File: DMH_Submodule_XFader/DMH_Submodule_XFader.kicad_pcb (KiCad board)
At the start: 2 copper layers, 37.5 x 62.5 mm, 47 parts, among them J1 Conn_01x08, J2 Conn_01x04, Q1 BC548, Q2 BC548, Q3 BC548, Q4 BC548, U1 TL074, U2 TL072

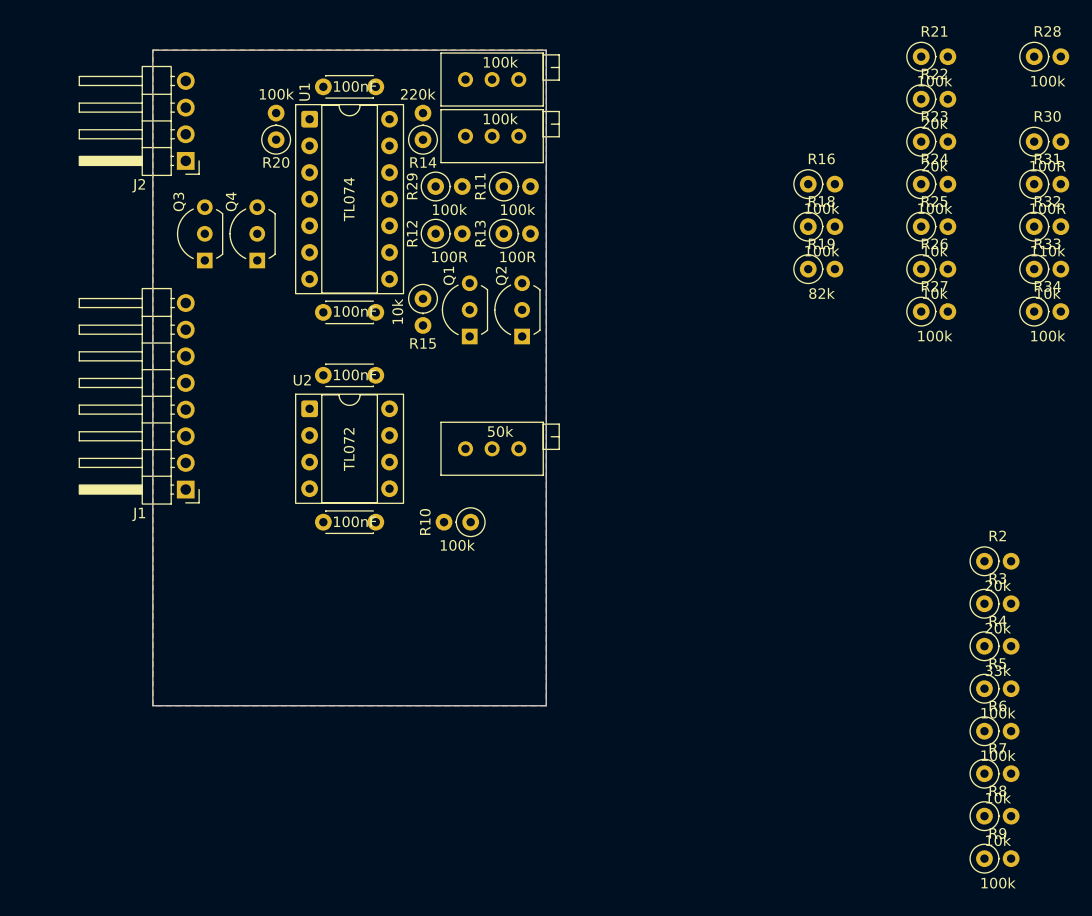
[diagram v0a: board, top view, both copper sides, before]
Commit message: Xfader comp placement done
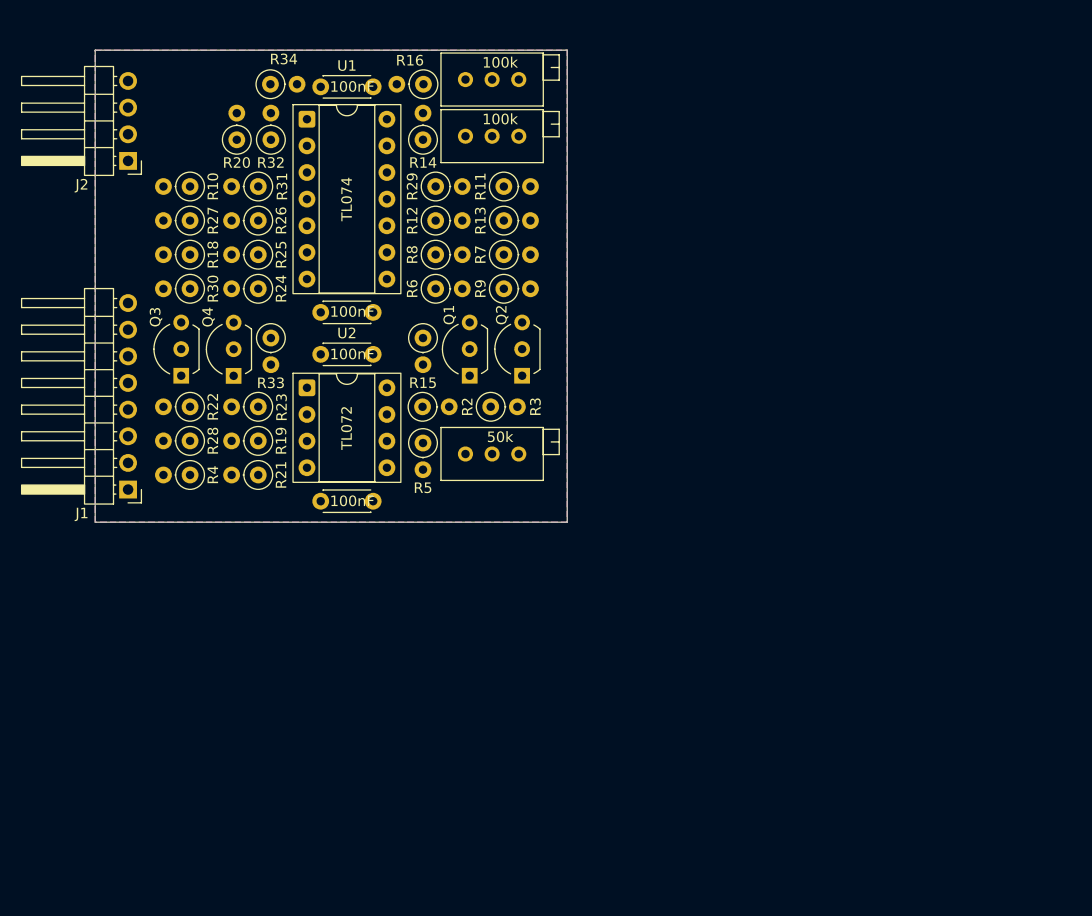
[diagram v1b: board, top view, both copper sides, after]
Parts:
- moved R28 88.4 mm to (63.5, 89.8), turned to 180 degrees
- moved R30 81.7 mm to (63.5, 75.2), turned to 180 degrees
- moved R4 77.5 mm to (63.5, 93.0), turned to 180 degrees
- moved R34 76.0 mm to (71.2, 55.8)
- moved R22 75.6 mm to (63.5, 86.5), turned to 180 degrees
- moved R8 74.8 mm to (87.0, 72.0)
- moved R21 74.7 mm to (70.0, 93.0), turned to 180 degrees
- moved R31 74.0 mm to (70.0, 65.5), turned to 180 degrees
- moved R32 73.2 mm to (71.2, 61.0), turned to 90 degrees
- moved R33 73.1 mm to (71.2, 79.9), turned to -90 degrees
- moved R9 71.1 mm to (93.5, 75.2)
- moved R27 70.2 mm to (63.5, 68.8), turned to 180 degrees
- moved R23 68.1 mm to (70.0, 86.5), turned to 180 degrees
- moved R7 67.4 mm to (93.5, 72.0)
- moved R6 67.2 mm to (87.0, 75.2)
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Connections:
- R18 pad 1: /Out A -> Net-(U2A--)
- R18 pad 2: Net-(U2A--) -> /Out A
- R2 pad 1: Net-(Q1-C) -> +12V
- R2 pad 2: +12V -> Net-(Q1-C)
- R21 pad 1: /Out A -> Net-(U2A--)
- R21 pad 2: Net-(U2A--) -> /Out A
- R22 pad 1: Net-(Q3-C) -> +12V
- R22 pad 2: +12V -> Net-(Q3-C)
- R23 pad 1: Net-(Q4-C) -> +12V
- R23 pad 2: +12V -> Net-(Q4-C)
- R3 pad 1: Net-(Q2-C) -> +12V
- R3 pad 2: +12V -> Net-(Q2-C)
- R4 pad 1: /CV Att In -> Net-(U2B--)
- R4 pad 2: Net-(U2B--) -> /CV Att In
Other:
- board size 37.5 x 62.5 mm -> 45 x 45 mm

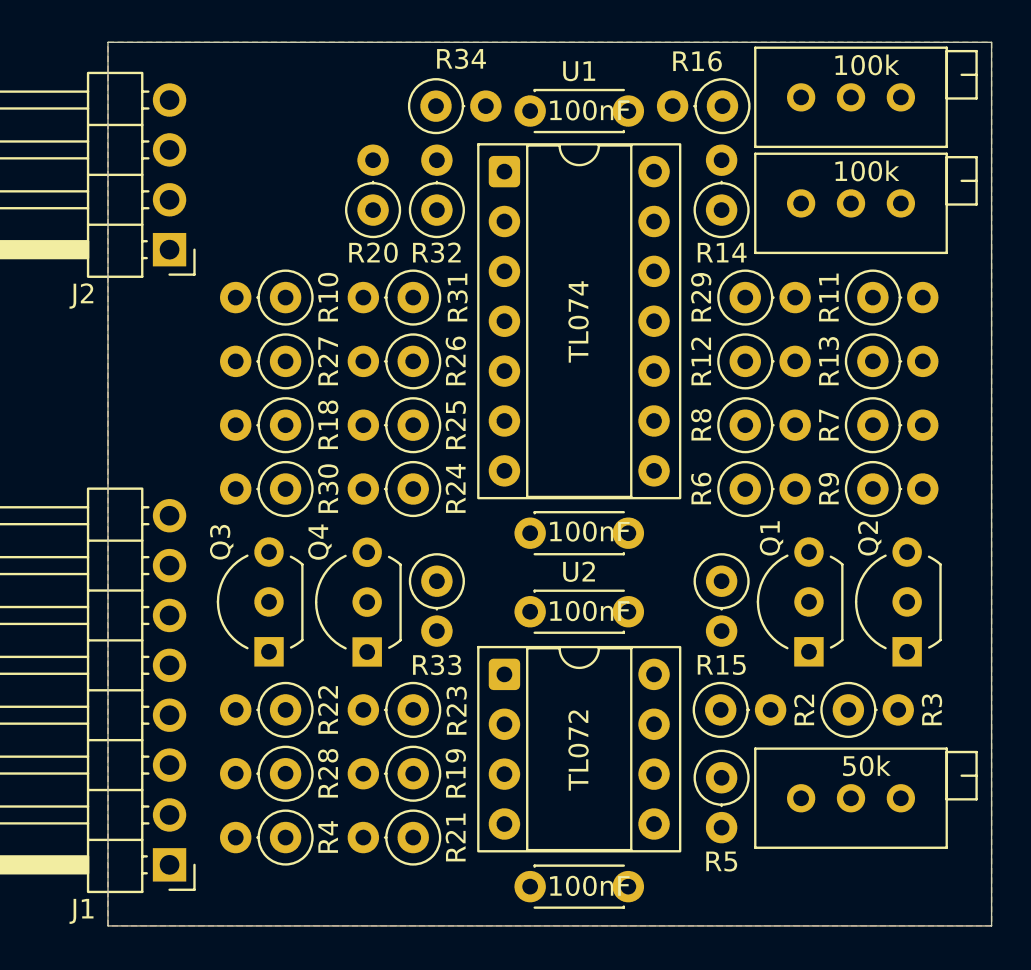
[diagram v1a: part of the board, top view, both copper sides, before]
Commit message: Xfader routing done
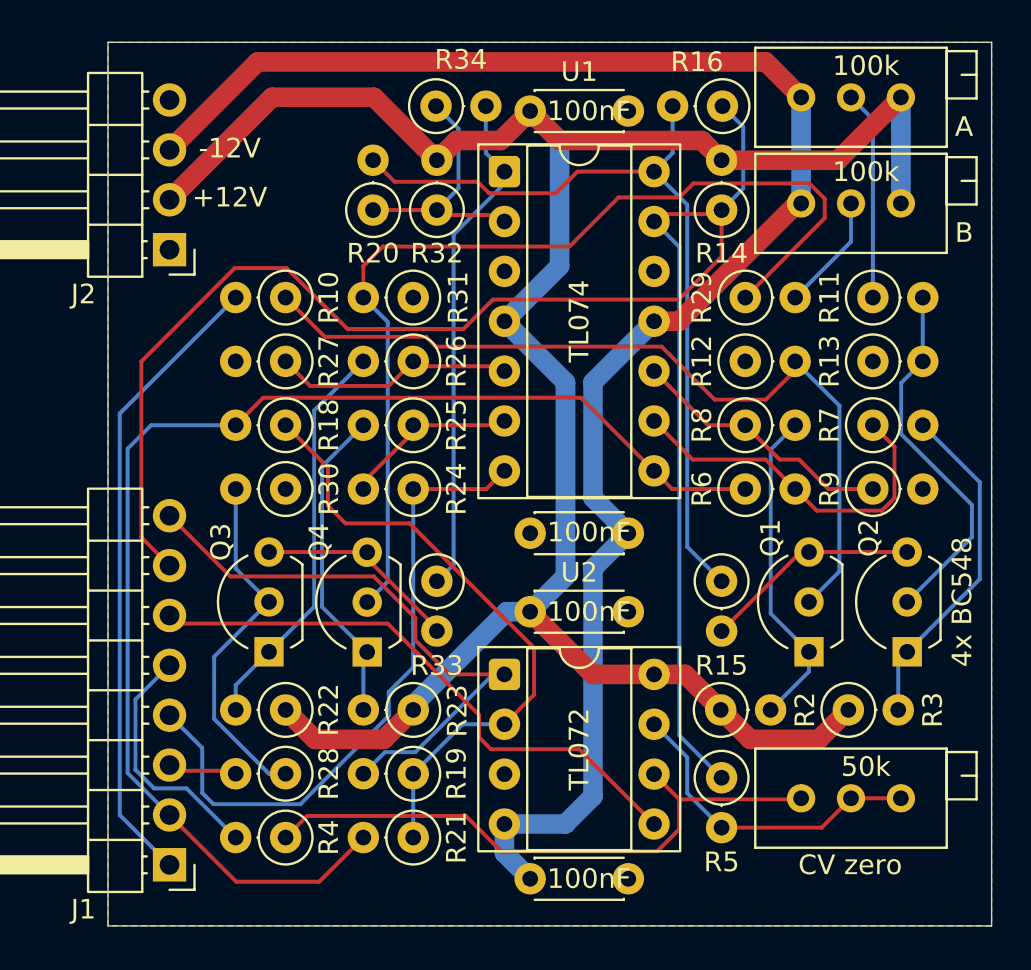
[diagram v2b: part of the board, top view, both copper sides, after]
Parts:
- moved C4 0.40 mm to (81.0, 95.1)
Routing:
- net +12V: track 0.00 -> 114.3 mm
- net /CV Mix In: track 0.00 -> 87.3 mm
- net -12V: track 0.00 -> 85.5 mm
- net /Out A: track 0.00 -> 66.2 mm
- net Net-(Q4-B): track 0.00 -> 50.3 mm
- net Net-(Q1-B): track 0.00 -> 43.0 mm
- net Net-(R15-Pad1): track 0.00 -> 41.5 mm
- net /Out B: track 0.00 -> 33.3 mm
- net /In A: track 0.00 -> 32.4 mm
- net Net-(U2A--): track 0.00 -> 31.9 mm
- net Net-(U2B--): track 0.00 -> 31.3 mm
- net /Out X: track 0.00 -> 30.3 mm
- net /CV Att Pot: track 0.00 -> 29.7 mm
- net Net-(R33-Pad1): track 0.00 -> 26.0 mm
- net Net-(Q3-C): track 0.00 -> 20.4 mm
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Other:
- board text added: "+12V"
- board text added: "-12V"
- board text added: "Mk1.0 - July 2026"
- board text removed: "Mk1.0 June 2026"

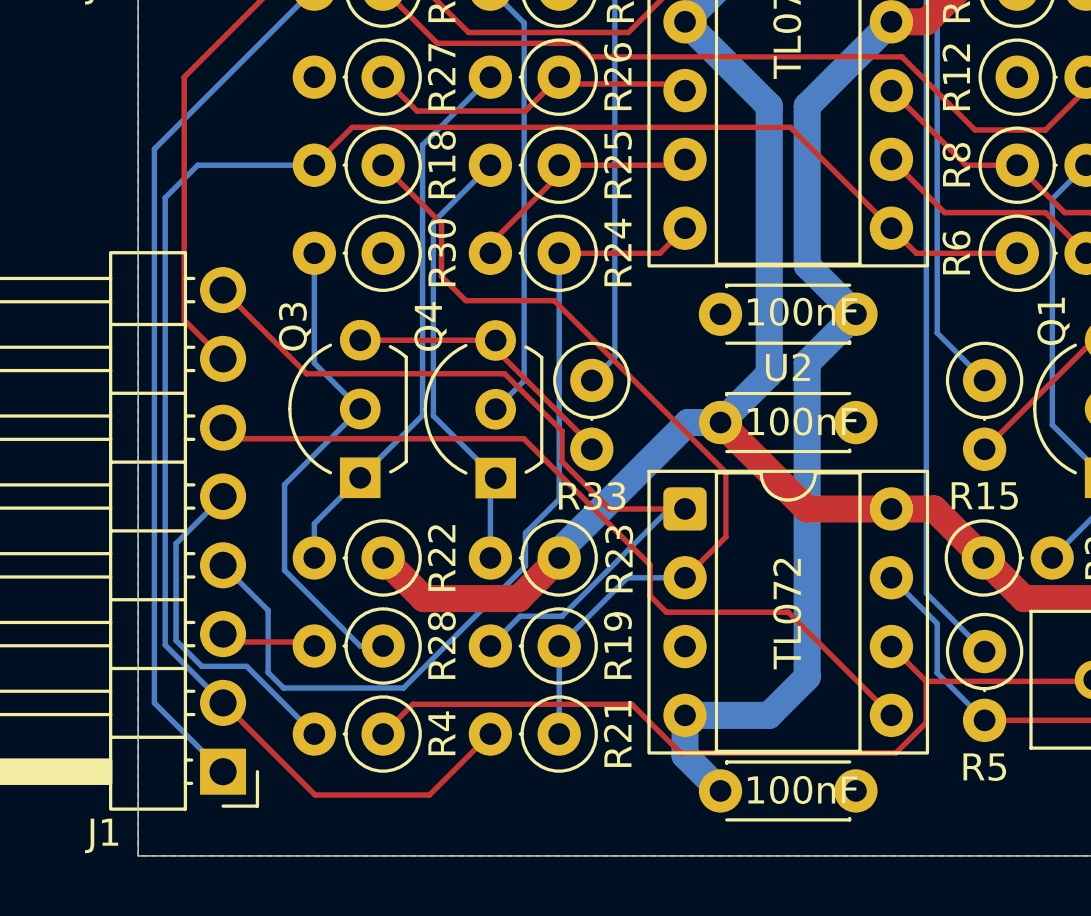
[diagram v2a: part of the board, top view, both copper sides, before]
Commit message: Fixed Out A and B mix labels and routing
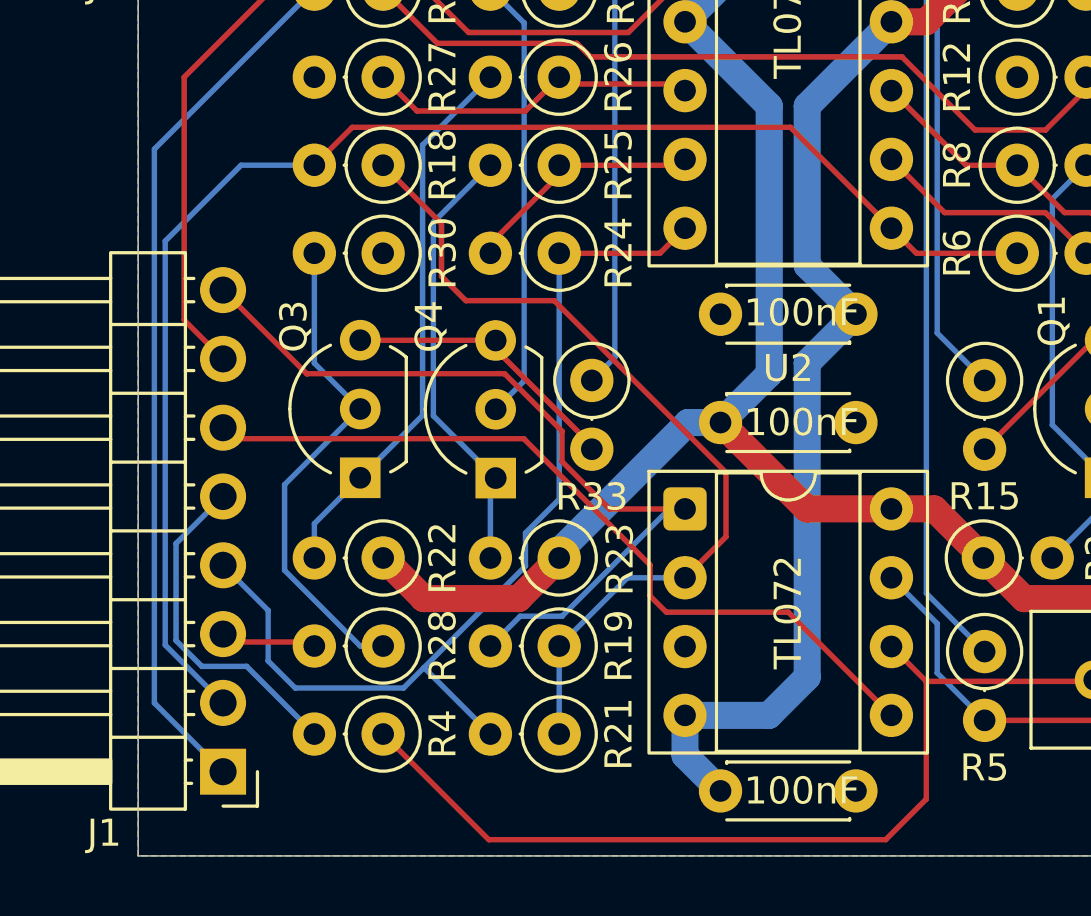
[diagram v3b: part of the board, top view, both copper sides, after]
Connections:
- net /CV Att In renamed /CV_Att_In
- net /CV Att Pot renamed /CV_Att_Pot
- net /CV Mix In renamed /CV_Mix_In
- net /In A renamed /In_A
- net /In B renamed /In_B
- net /Out X renamed /Out_X
- J1 pad 2: /Out A -> /Out_A
- J1 pad 4: /Out B -> /Out_B
- R18 pad 2: /Out A -> /Out_A
- R21 pad 2: /Out A -> /Out_B
- R24 pad 1: /Out B -> /Out_B
- R6 pad 1: /Out A -> /Out_A
- U1 pad 7: /Out B -> /Out_B
- U1 pad 8: /Out A -> /Out_A
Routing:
- net /Out A: track 66.2 -> 0.00 mm
- net /Out_A: track 0.00 -> 53.1 mm
- net /Out_B: track 0.00 -> 36.6 mm
- net /Out B: track 33.3 -> 0.00 mm
- net Net-(U2B--): track 31.3 -> 34.7 mm

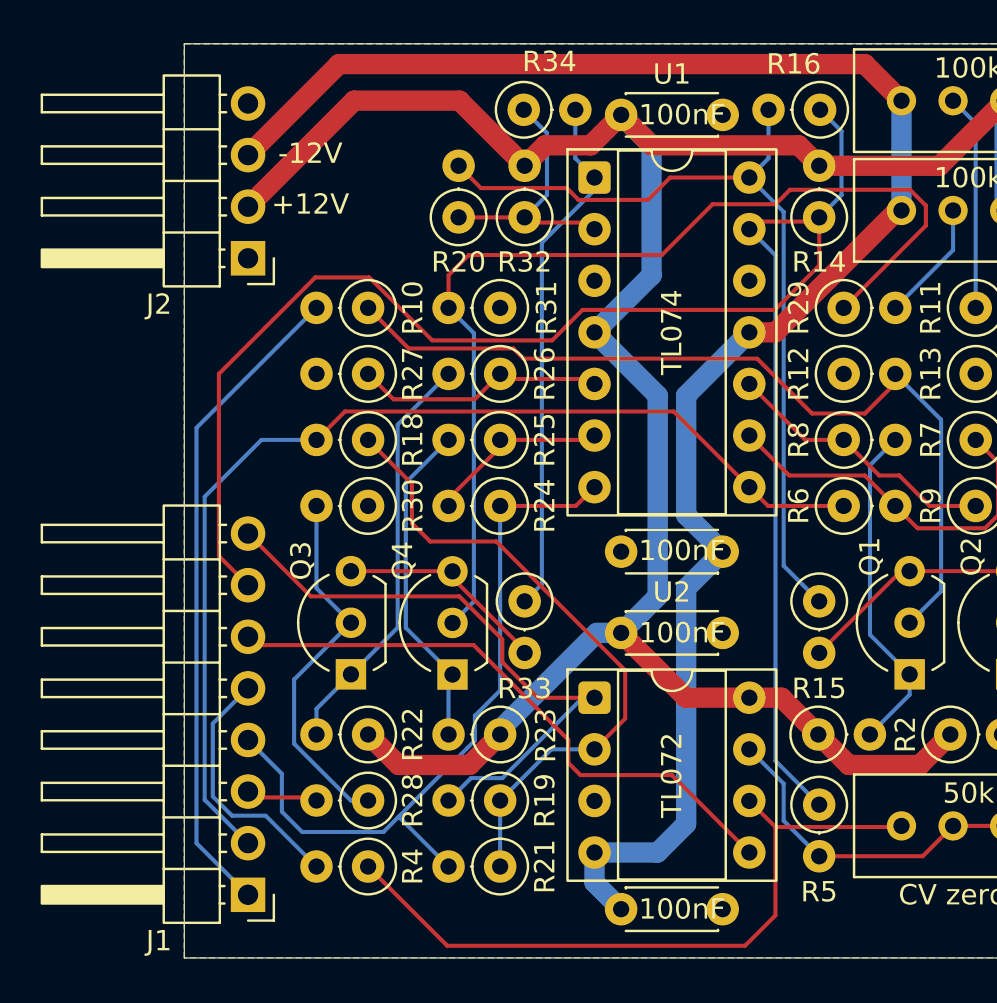
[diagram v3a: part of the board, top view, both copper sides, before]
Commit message: Made connector breadboard compatible
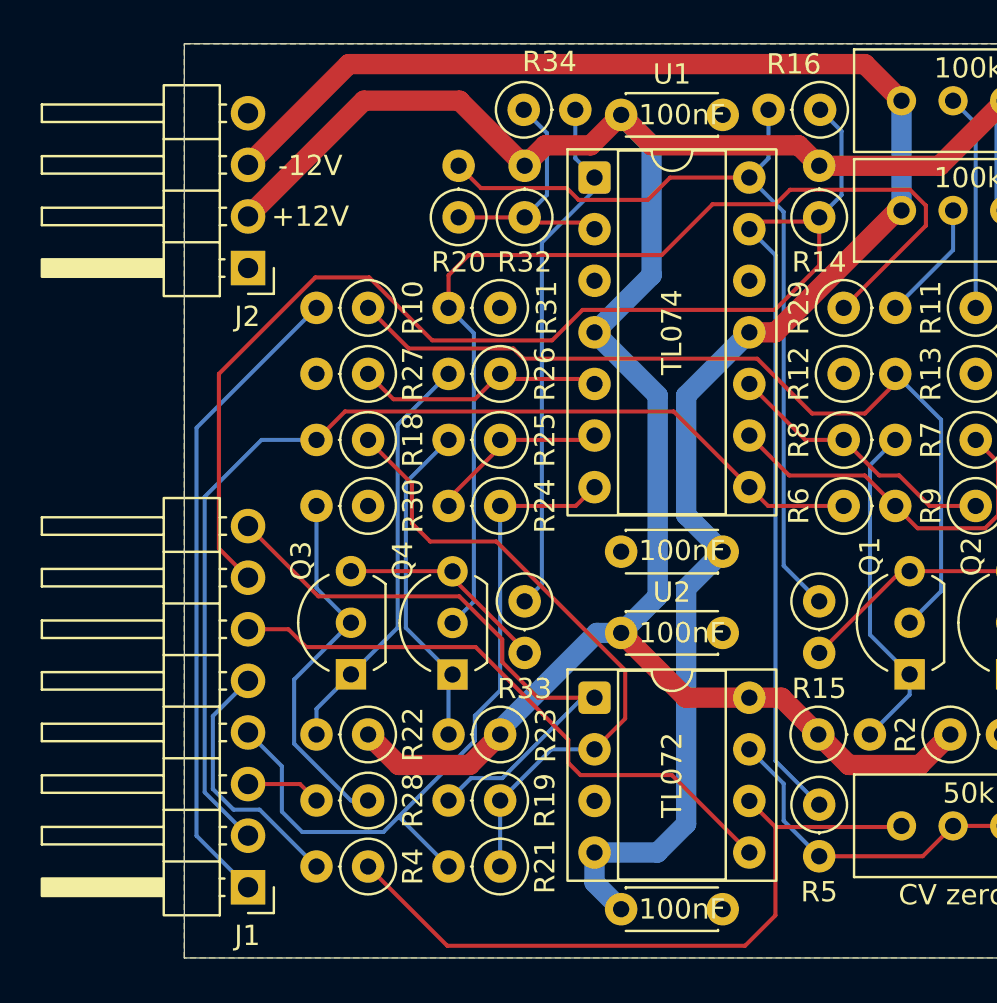
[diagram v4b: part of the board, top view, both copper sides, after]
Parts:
- moved J2 0.48 mm to (57.6, 63.5)
- moved J1 0.37 mm to (57.6, 94.0)

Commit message: Swapped J1 and J2 tags around on XFader SM
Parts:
- renumbered J2 to J1, J1 to J2
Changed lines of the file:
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@@
 	(paper "A4" portrait)
 	(title_block
+		(title "Cross Fader Submodule")
+		(date "2026-07-15")
 		(rev "1")
 		(company "DMH Instruments")
-		(comment 1 "10cm Kosmo format synthesizer module PCB")
+		(comment 1 "Submodule PCB for Kosmo format synthesizer module")
 	)
 	(layers
@@
 		(descr "Through hole angled pin header, 1x08, 2.54mm pitch, 6mm pin length, single row")
 		(tags "Through hole angled pin header THT 1x08 2.54mm single row")
-		(property "Reference" "J1"
+		(property "Reference" "J2"
 			(at 0.035 -2.38 0)
 			(layer "F.SilkS")
@@
 		(descr "Through hole angled pin header, 1x04, 2.54mm pitch, 6mm pin length, single row")
 		(tags "Through hole angled pin header THT 1x04 2.54mm single row")
-		(property "Reference" "J2"
+		(property "Reference" "J1"
 			(at 0.035 -2.39 0)
 			(layer "F.SilkS")
@@
 		)
 	)
+	(group "VC_Cross_Fader_SC"
+		(lib_id "SynthStuff:VC_Cross_Fader_SC")
+		(members "156aba6d-8716-4206-91db-de05616f5240" "15aec086-26ae-4e8f-a86d-fc440ad5c0df"
+			"1bb2db6c-582a-4b0e-8f4b-40b66a64ff61" "1fbbc819-05f1-47c2-8f1f-3bb8db341822"
+			"2b17a480-4af7-4e7f-991c-c097a11cd05d" "2e6d8948-6522-4f16-a307-ca4d9cc91755"
+			"30a23566-8bf4-4b6c-9b6a-75067ad19441" "369e710e-8de4-4dfb-ba15-73f4a77e019f"
+			"3956684d-cae4-4243-94fb-70f2736e98bc" "3d31149a-1864-4833-a03c-665f6cdabaeb"
+			"4461cd04-9275-4659-b197-4b0a686f2318" "56fed60b-4643-4708-9870-a6b837a88053"
+			"579d0aa6-73d9-4fb3-8abd-fc4274f45e4c" "583ccfeb-c872-4696-8f8f-0a6ca50f942c"
+			"5cca8f87-57cb-4272-b579-1a8804907ffc" "62c581da-ec56-4d57-96db-f129a8c06fc2"
+			"6a76fc0e-b09a-4e82-a521-1a4951e7ec7f" "6addff73-f2e9-4120-810d-7575553e364f"
+			"6c44f2a9-b4d8-40ea-8808-e1d65c021900" "7ae55dee-329c-4567-90b2-6424e93c5628"
+			"7bda555e-0de3-4edf-9854-241fcc90ec5e" "7c7e3e80-d168-4189-b051-6f808cd3f5fb"
+			"8320bda0-bc39-43a6-bfd5-06237ac0b623" "83eb8756-2e68-4a08-b851-e0782be10ee8"
+			"943f40ae-fc1c-4c4e-94ca-81dc930d78a3" "a59fb55c-dbe2-459e-b66d-08ceac7bc7c9"
+			"a6847c59-0b88-4466-8f82-91429cfb9da5" "a7a44be9-6090-4319-bec9-8a12132698da"
+			"ab5b8e30-2d71-4c6c-80ac-5a0302db4a4d" "ae2c829e-c655-4923-9b2f-7120f49f37bf"
+			"afca08c2-80c1-43d7-a743-0dc600a95ba6" "b1e27e14-d0ae-422f-8d6e-d1a523b2b754"
+			"b31ed478-7adb-466e-8d2f-699db136c7fa" "b9ee7b7e-a13e-4061-a12f-e3fcc1a05ca6"
+			"bce84751-ac23-4f29-8e5b-f7fc7d983cce" "c82e422e-f4c9-487b-a626-ad07bfc0854c"
+			"ca2998d3-202b-48cb-b112-83c1974e139a" "d63632fb-12e3-44c3-870f-47094aa139c1"
+			"d764697f-4978-448c-ae33-f1167d715a5b" "d9cee89f-b31c-41ec-8999-375c455e500d"
+			"ddebb524-a01e-48f0-9f1e-0a30325e7d16" "e8fcf28e-4c9d-4f11-a848-cb953976e413"
+			"e94f4345-b8fb-4abc-9fc7-42fb7c7bc8f3" "fc67f0af-7d82-489c-b288-521ec357eebf"
+			"ff8c768b-9eea-4238-a85c-2a25bcef61ad"
+		)
+	)
